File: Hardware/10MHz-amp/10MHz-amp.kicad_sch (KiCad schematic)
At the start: 65 parts, among them J1 Conn_Coaxial, J3 Conn_Coaxial, J4 Barrel_Jack_MountingPin, K1 TQ2-24V, K2 TQ2-24V, K3 TQ2-24V, K4 TQ2-24V, K5 TQ2-24V, Q1 PMOS, SW1 SW_SP5T_NR01105, SW2 SW_SPDT, U1 THS3491xDDA

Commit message: added power management circuit
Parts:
- added C11, C12: 10u, Capacitor_SMD:C_0603_1608Metric, symbol Device:C
- added C19, C20: 6.8u, Capacitor_SMD:C_0603_1608Metric, symbol Device:C
- added C21, C22, C23, C24, C25, C26: 100n, Capacitor_SMD:C_0603_1608Metric, symbol Device:C
- added C27: 1u, Capacitor_SMD:C_0603_1608Metric, symbol Device:C
- added C8, C9: 22u, Capacitor_SMD:C_0603_1608Metric, symbol Device:C
- added D1, D2: PTVS15VZ1USK, Diode_SMD:Nexperia_DSN1608-2_1.6x0.8mm, symbol Diode:PTVS15VZ1USK
- added D10, D21, D22, D7, D9: LED, Diode_SMD:D_0603_1608Metric, symbol Device:LED
- added D4, D5: D_Zener, Diode_SMD:D_0603_1608Metric, symbol Device:D_Zener
- added F1, F2: Fuse, symbol Device:Fuse
- added J2, J3: BANANA_JACK, symbol Connector:Conn_01x01_Socket
- added J6: Conn_01x07_Pin, Connector_PinHeader_2.54mm:PinHeader_1x07_P2.54mm_Horizontal, symbol Connector:Conn_01x07_Pin
- added J7: Conn_01x07_Socket, Connector_PinSocket_2.54mm:PinSocket_1x07_P2.54mm_Vertical, symbol Connector:Conn_01x07_Socket
- added J9: Conn_01x01_Socket, symbol Connector:Conn_01x01_Socket
- added JP2: Jumper_2_Bridged, symbol Jumper:Jumper_2_Bridged
- added Q1: PMOS, symbol Simulation_SPICE:PMOS
- added Q2: NMOS, symbol Simulation_SPICE:NMOS
- added Q4, Q5: AO4803A, SO8SOP-8L_AOS, symbol 2025-08-14_00-39-45:AO4803A
- added R10, R15, R16, R35, R36, R37, R7, R8: 10k, Capacitor_SMD:C_0603_1608Metric, symbol Device:R
- added R27, R28, R29, R30, R31, R32, R33, R34: 1M, Capacitor_SMD:C_0603_1608Metric, symbol Device:R
- added R38, R39: 0, symbol Device:R
- added SW3: SW_SPDT, symbol Switch:SW_SPDT
- added U2: LTC4417HGN, Package_SO:SSOP-24_3.9x8.7mm_P0.635mm, symbol Power_Management:LTC4417HGN
- C1: renamed from C3; footprint (none) -> Capacitor_SMD:C_0603_1608Metric
- C10: renamed from C5; footprint (none) -> Capacitor_SMD:C_0603_1608Metric
- C13: renamed from C6; footprint (none) -> Capacitor_SMD:C_0603_1608Metric
- C14: renamed from C7; footprint (none) -> Capacitor_SMD:C_0603_1608Metric
- C15: renamed from C8; footprint (none) -> Capacitor_SMD:C_0603_1608Metric
- C16: renamed from C9; footprint (none) -> Capacitor_SMD:C_0603_1608Metric
- C17: renamed from C10; footprint (none) -> Capacitor_SMD:C_0603_1608Metric
- C18: renamed from C11; footprint (none) -> Capacitor_SMD:C_0603_1608Metric
- C2, R11, R4, R5, R6, R9: footprint (none) -> Capacitor_SMD:C_0603_1608Metric
- C3: renamed from C1; footprint (none) -> Capacitor_SMD:C_0603_1608Metric
- C4: renamed from C12; footprint (none) -> Capacitor_SMD:C_0603_1608Metric
- C5: renamed from C13; footprint (none) -> Capacitor_SMD:C_0603_1608Metric
- C6: renamed from C14; footprint (none) -> Capacitor_SMD:C_0603_1608Metric
- C7: renamed from C4; footprint (none) -> Capacitor_SMD:C_0603_1608Metric
- D11: renamed from D7; footprint (none) -> Diode_SMD:D_0603_1608Metric
- D12: renamed from D6; footprint (none) -> Diode_SMD:D_0603_1608Metric
- D13: renamed from D5; footprint (none) -> Diode_SMD:D_0603_1608Metric
- D14: renamed from D4; footprint (none) -> Diode_SMD:D_0603_1608Metric
- D15: renamed from D3; footprint (none) -> Diode_SMD:D_0603_1608Metric
- D16: renamed from D9; footprint (none) -> Diode_SMD:D_0603_1608Metric; Notes (none) -> ADJ GAIN
- D17: renamed from D10; footprint (none) -> Diode_SMD:D_0603_1608Metric; Notes (none) -> 2x
- D18: renamed from D11; footprint (none) -> Diode_SMD:D_0603_1608Metric; Notes (none) -> 10x
- D19: renamed from D12; footprint (none) -> Diode_SMD:D_0603_1608Metric; Notes (none) -> 50x
- D20: renamed from D13; footprint (none) -> Diode_SMD:D_0603_1608Metric; Notes (none) -> 100x
- D6: renamed from D1; footprint (none) -> Diode_SMD:D_0603_1608Metric
- D8: footprint (none) -> Diode_SMD:D_0603_1608Metric; Notes (none) -> POWER
- JP1: value star_point -> Jumper_2_Bridged
- N1: value Housing_Pad -> Housing
- R1: renamed from R8; footprint (none) -> Capacitor_SMD:C_0603_1608Metric; Notes (none) -> LOAD RESISTOR 18w
- R12: renamed from R7; footprint (none) -> Capacitor_SMD:C_0603_1608Metric
- R13: renamed from R10; footprint (none) -> Capacitor_SMD:C_0603_1608Metric
- R14: renamed from R16; footprint (none) -> Capacitor_SMD:C_0603_1608Metric
- R17: renamed from R1; footprint (none) -> Capacitor_SMD:C_0603_1608Metric
- R18: renamed from R12; footprint (none) -> Capacitor_SMD:C_0603_1608Metric
- R19: renamed from R13; footprint (none) -> Capacitor_SMD:C_0603_1608Metric
- R2: renamed from R3; footprint (none) -> Potentiometer_THT:Potentiometer_Alps_RK09Y11_Single_Horizontal
- R20: renamed from R14; footprint (none) -> Capacitor_SMD:C_0603_1608Metric
- R21: renamed from R15; footprint (none) -> Capacitor_SMD:C_0603_1608Metric
- R22: renamed from R17; footprint (none) -> Capacitor_SMD:C_0603_1608Metric
- R23: renamed from R18; footprint (none) -> Capacitor_SMD:C_0603_1608Metric
- R24: renamed from R19; footprint (none) -> Capacitor_SMD:C_0603_1608Metric
- R25: renamed from R20; footprint (none) -> Capacitor_SMD:C_0603_1608Metric
- R26: renamed from R21; footprint (none) -> Capacitor_SMD:C_0603_1608Metric
- R3: renamed from R2; footprint (none) -> Capacitor_SMD:C_0603_1608Metric
- renumbered D2 to D3, F1 to F3, J3 to J5, JP2 to JP3, Q1 to Q3, SW2 to SW1, SW1 to SW2
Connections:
- net +24V: now also C23.1, C26.1, J7.1 (Pin_1), Q5.7, Q5.8, R29.2, U2.23 (V2); no longer C1.1, C18.1, C2.1, C3.1, R12.2, SW2.C (Common), U1.7 (V+)
- net -VDC: now also C12.2, C9.2, D10.1 (K), JP2.2 (B); no longer C1.2, C10.2, C13.2, C14.2, C15.2, C16.2, C17.2, C18.2, C2.2, C3.2, C4.1, C4.2, C5.1, C5.2, C6.1, C6.2, C7.2, D3.3 (A), J1.2 (Ext), J4.2, J5.2 (Ext), JP1.1 (A), R1.2, R14.1, R17.1, R18.1, R19.1, R2.2, R20.1, R21.1, R22.1, R23.1, R24.1, R25.1, R26.1, R3.2, R4.2, R5.2, R6.2, R9.1, SW1.3 (C), U1.1 (REF), U1.4 (V-), U1.9 (EP)
- net GNDS: now also R38.1
- net at C17.1, D15.1 (K), D20.2 (A)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: now also J7.6 (Pin_6); no longer SW2.5
- net at C16.1, D14.1 (K), D19.2 (A)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: now also J7.5 (Pin_5); no longer SW2.4
- net at R1.1, U1.3 (+): now also C27.2; no longer J1.1 (In)
- net at C13.1, D11.1 (K), D16.2 (A)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: now also J7.2 (Pin_2); no longer SW2.1
- net at SW1.2 (B), U1.8 (~{PD}): now also D7.2 (A)
- net at C14.1, D12.1 (K), D17.2 (A)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: now also J7.3 (Pin_3); no longer SW2.2
- net at C15.1, D13.1 (K), D18.2 (A)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: now also J7.4 (Pin_4); no longer SW2.3
- net at SW2.MP: now also J6.7 (Pin_7); no longer JP1.2 (B)
- new net: Q4.1, Q4.3, U2.21 (VS1)
- new net: C21.1, Q4.2, Q4.4, U2.20 (G1)
- new net: D9.1 (K), R15.2
- new net: D4.1 (K), JP1.1 (A), Q1.3 (S)
- new net: J6.2 (Pin_2), SW2.1
- new net: J6.3 (Pin_3), SW2.2
- new net: J6.4 (Pin_4), SW2.3
- new net: J6.5 (Pin_5), SW2.4
- new net: J6.6 (Pin_6), SW2.5
- new net: C18.1, J6.1 (Pin_1), SW2.C (Common)
- new net: C22.1, Q5.2, Q5.4, U2.18 (G2)
- new net: SW3.2 (B), U2.2 (~{SHDN})
- new net: R37.2, SW3.3 (C)
- new net: D10.2 (A), R16.1
- new net: D21.2 (A), R35.1
- new net: R28.1, R35.2, U2.11 (~{VALID2})
- new net: C24.2, R32.1, R34.2, U2.5 (OV1)
- new net: F2.2, Q2.1 (D)
- new net: D5.1 (K), Q2.2 (G), R8.1
- new net: D5.2 (A), JP2.1 (A), Q2.3 (S)
- new net: J9.1 (Pin_1), R39.2
- new net: D7.1 (K), R10.2
- new net: D2.1 (K), F2.1, J3.1 (Pin_1)
- new net: R27.1, R36.2, U2.10 (~{VALID1})
- new net: Q5.1, Q5.3, U2.19 (VS2)
- new net: R31.1, R32.2, U2.4 (UV1)
- new net: R29.1, R30.2, U2.6 (UV2)
- new net: C23.2, R30.1, R33.2, U2.7 (OV2)
- new net: D22.2 (A), R36.1
- new net: D1.2 (A), F1.1, J2.1 (Pin_1)
- new net: F1.2, Q1.1 (D)
- new net: D4.2 (A), Q1.2 (G), R7.2
- new net: C27.1, J1.1 (In)
- new net +VDC: C11.1, C24.1, C25.1, C8.1, D9.2 (A), JP1.2 (B), Q4.7, Q4.8, R31.2, U2.24 (V1)
- new net GND: C1.2, C10.2, C11.2, C12.1, C13.2, C14.2, C15.2, C16.2, C17.2, C18.2, C19.2, C2.2, C20.2, C21.2, C22.2, C25.2, C26.2, C3.2, C4.2, C5.2, C6.2, C7.2, C8.2, C9.1, D1.1 (K), D2.2 (A), D21.1 (K), D22.1 (K), D3.3 (A), J1.2 (Ext), J4.2, J5.2 (Ext), J7.7 (Pin_7), R1.2, R10.1, R14.1, R15.1, R16.2, R17.1, R18.1, R19.1, R2.2, R20.1, R21.1, R22.1, R23.1, R24.1, R25.1, R26.1, R3.2, R33.1, R34.1, R37.1, R38.2, R39.1, R4.2, R5.2, R6.2, R7.1, R8.2, R9.1, SW1.3 (C), U1.1 (REF), U1.9 (EP), U2.13 (GND), U2.16 (G3), U2.17 (VS3), U2.22 (V3), U2.3 (HYS), U2.8 (UV3), U2.9 (OV3)
- new net VCC: C1.1, C19.1, C2.1, C20.1, C3.1, Q4.5, Q4.6, Q5.5, Q5.6, R12.2, R27.2, R28.2, U1.7 (V+), U2.15 (VOUT)
- new net VS: C4.1, C5.1, C6.1, U1.4 (V-)
- no-connect marks 21 -> 23
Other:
- note added: "24v @ 2A INPUT"
- note added: "DUAL RAIL +-15VMAX @ 500mA INPUT"
- note added: "POWER AMP 100MHz 30V pk-pk 500mA 50OHM LOAD"
- note added: "POWER SELECTOR"
- note added: "STAR GROUND POINT"
- moved on the sheet: C1, C10, C13, C14, C15, C16, C17, C18, C2, C3, C4, C5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

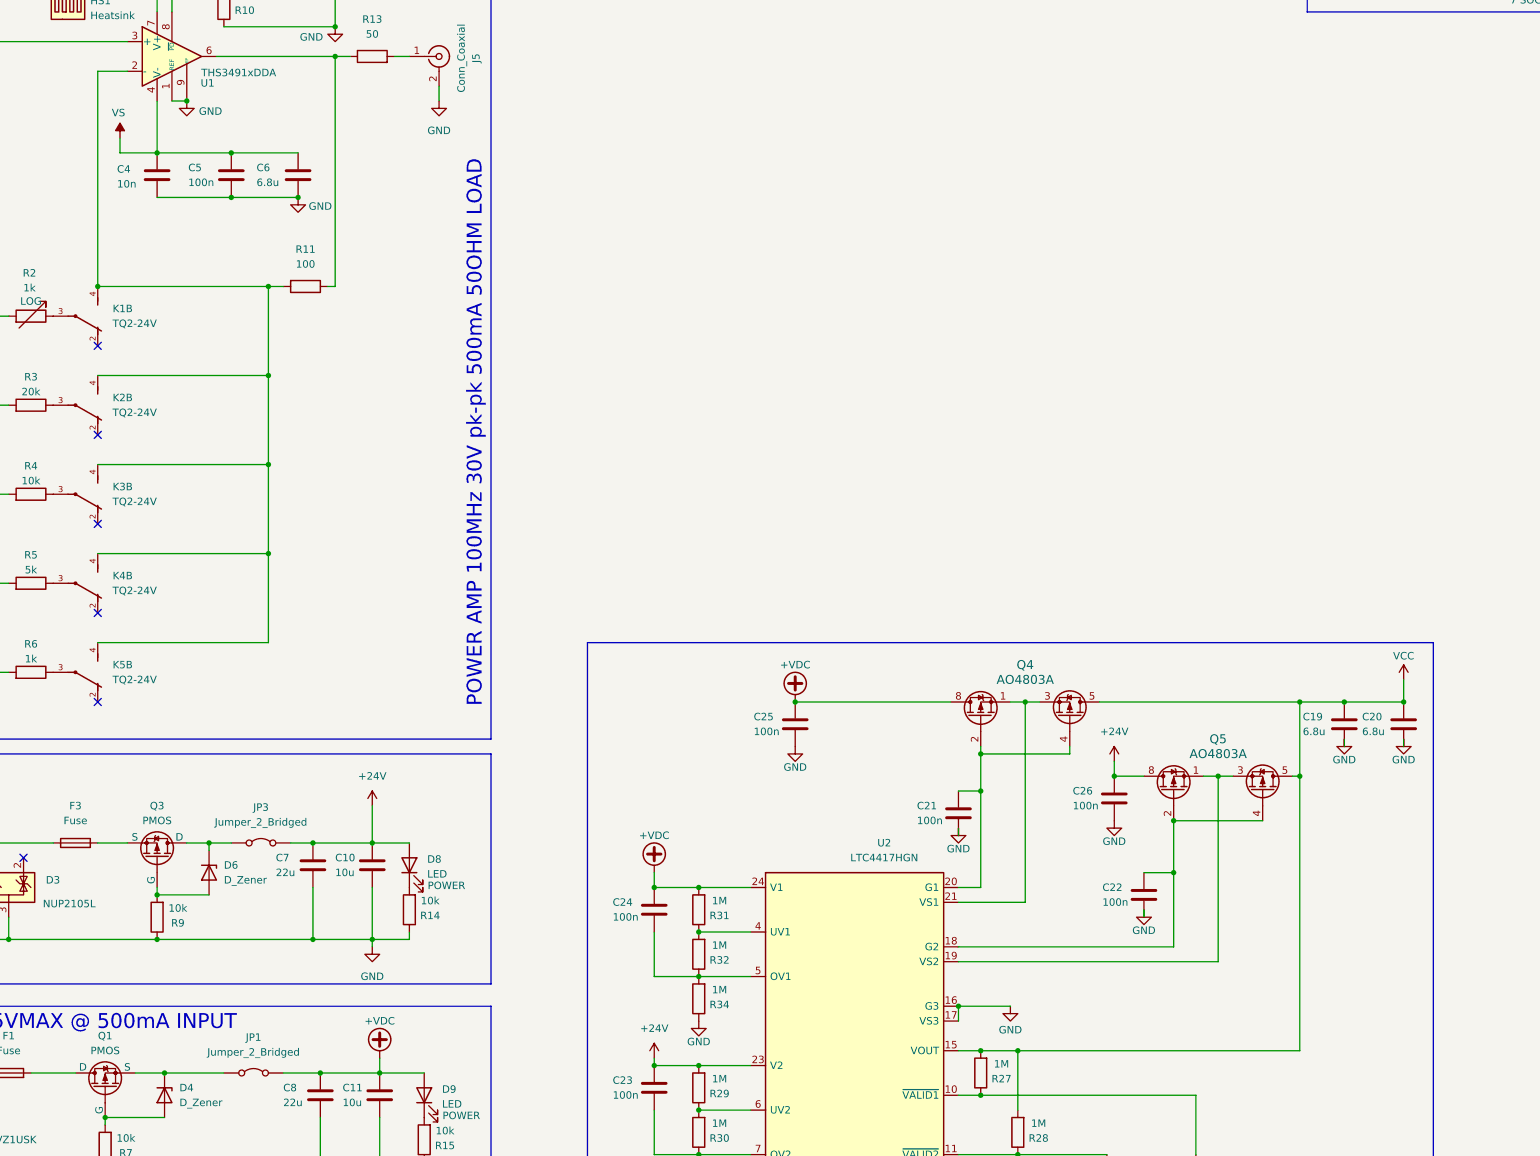
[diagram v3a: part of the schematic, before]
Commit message: added VS switcher circuit, so when +VDC is present then VS == -VDC if +VDC is not present then VS == GND
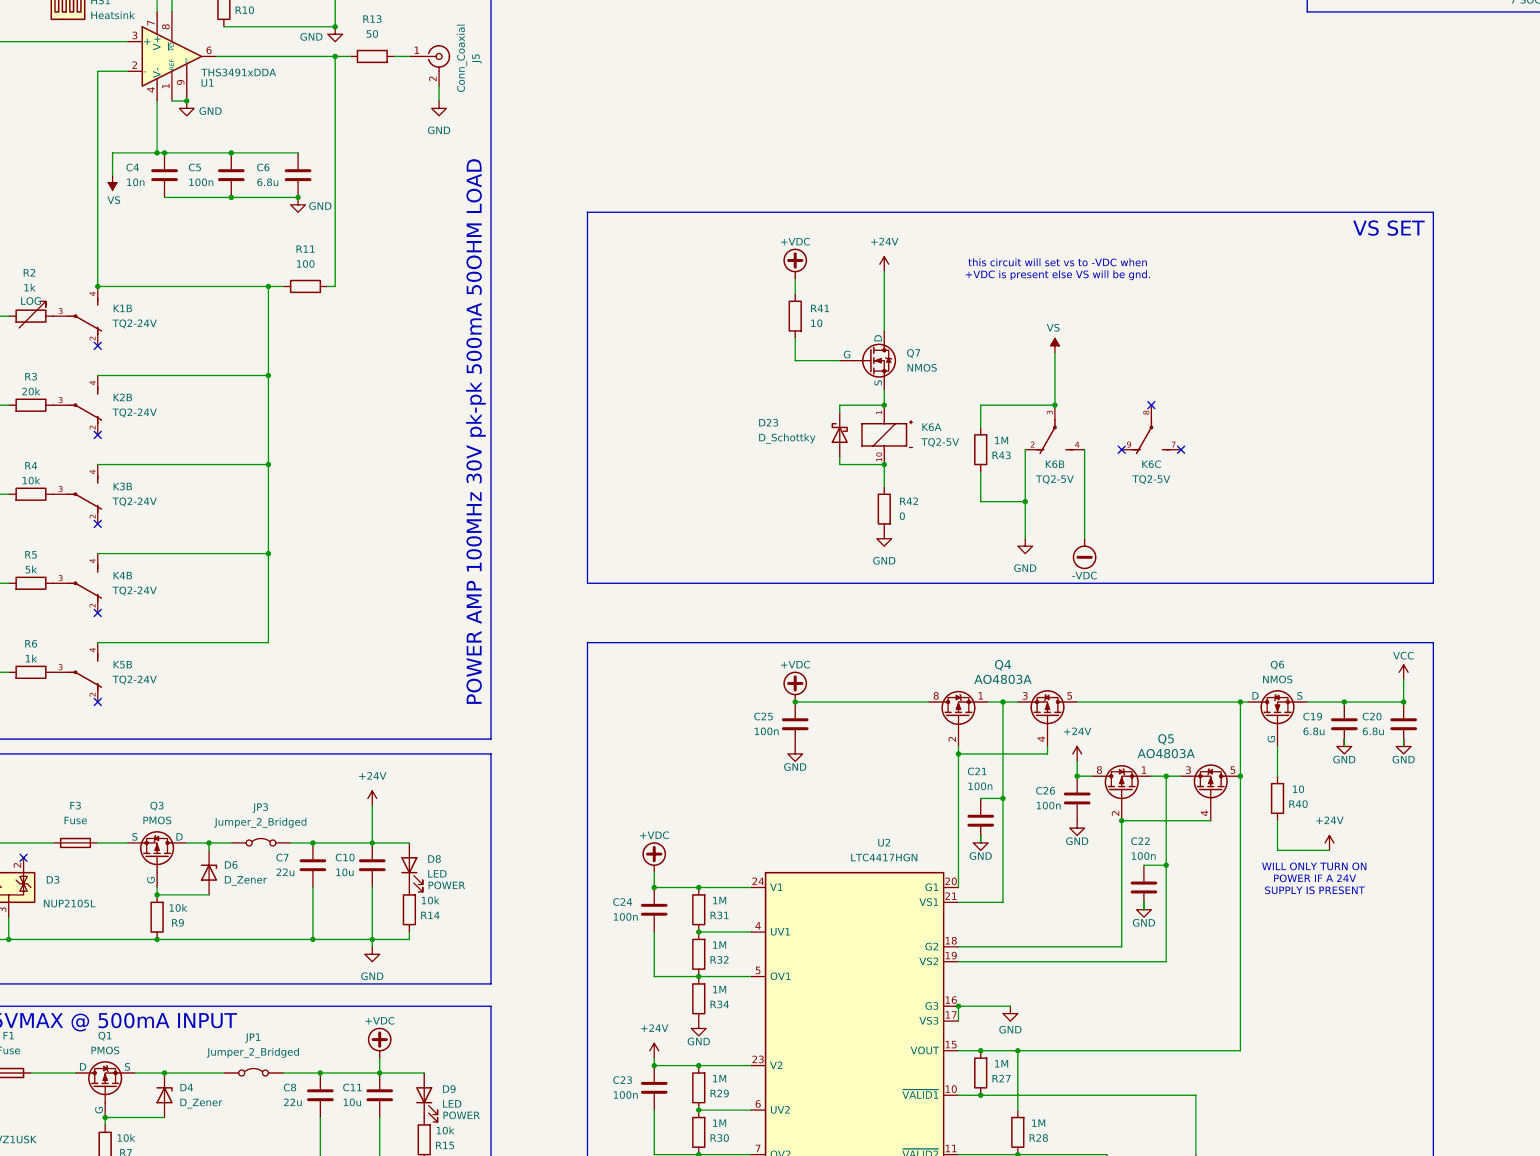
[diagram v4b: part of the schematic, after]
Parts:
- added D23: D_Schottky, Diode_SMD:D_0603_1608Metric, symbol Device:D_Schottky
- added K6: TQ2-5V, TQ2-5V:TQ2, symbol TQ2-5V:TQ2-5V
- added Q6, Q7: NMOS, symbol Simulation_SPICE:NMOS
- added R40, R41: 10, Capacitor_SMD:C_0603_1608Metric, symbol Device:R
- added R42: 0, Capacitor_SMD:C_0603_1608Metric, symbol Device:R
- added R43: 1M, Capacitor_SMD:C_0603_1608Metric, symbol Device:R
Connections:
- net +24V: now also Q7.1 (D), R40.1
- net +VDC: now also R41.1
- net -VDC: now also K6.4
- net GND: now also K6.2, R42.2, R43.1
- net VCC: now also Q6.3 (S); no longer Q4.5, Q4.6, Q5.5, Q5.6, R27.2, R28.2, U2.15 (VOUT)
- net VS: now also K6.3, R43.2
- net at Q4.1, Q4.3, U2.21 (VS1): now also C21.1
- net at Q4.2, Q4.4, U2.20 (G1): no longer C21.1
- net at Q5.2, Q5.4, U2.18 (G2): no longer C22.1
- net at Q5.1, Q5.3, U2.19 (VS2): now also C22.1
- new net: D23.1 (K), K6.1, Q7.3 (S)
- new net: D23.2 (A), K6.10, R42.1
- new net: Q4.5, Q4.6, Q5.5, Q5.6, Q6.1 (D), R27.2, R28.2, U2.15 (VOUT)
- new net: Q6.2 (G), R40.2
- new net: Q7.2 (G), R41.2
- no-connect marks 23 -> 26
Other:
- note added: "VS SET"
- note added: "WILL ONLY TURN ON POWER IF A 24V SUPPLY IS PRESENT"
- note added: "this circuit will set vs to -VDC when +VDC is present else VS will be gnd."
- moved on the sheet: C21, C22, C26, C4, Q4, Q5

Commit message: removed power swapping circuit and replaced with switch and relay because it was going to be too much to a pain to make work
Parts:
- removed C19, C20: 6.8u, Capacitor_SMD:C_0603_1608Metric, symbol Device:C
- removed C21, C22, C24, C25, C26: 100n, Capacitor_SMD:C_0603_1608Metric, symbol Device:C
- removed C27: 1u, Capacitor_SMD:C_0603_1608Metric, symbol Device:C
- removed C8: 22u, Capacitor_SMD:C_0603_1608Metric, symbol Device:C
- removed D1, D2: PTVS15VZ1USK, Diode_SMD:Nexperia_DSN1608-2_1.6x0.8mm, symbol Diode:PTVS15VZ1USK
- removed D21, D22: LED, Diode_SMD:D_0603_1608Metric, symbol Device:LED
- removed D3: NUP2105L, Package_TO_SOT_SMD:SOT-23, symbol Power_Protection:NUP2105L
- removed J9: Conn_01x01_Socket, symbol Connector:Conn_01x01_Socket
- removed Q4, Q5: AO4803A, SO8SOP-8L_AOS, symbol 2025-08-14_00-39-45:AO4803A
- removed Q6, Q7: NMOS, symbol Simulation_SPICE:NMOS
- removed R27, R28, R29, R30, R33, R34, R43: 1M, Capacitor_SMD:C_0603_1608Metric, symbol Device:R
- removed R35, R36, R37: 10k, Capacitor_SMD:C_0603_1608Metric, symbol Device:R
- removed R40, R41: 10, Capacitor_SMD:C_0603_1608Metric, symbol Device:R
- removed SW3: SW_SPDT, symbol Switch:SW_SPDT
- removed U2: LTC4417HGN, Package_SO:SSOP-24_3.9x8.7mm_P0.635mm, symbol Power_Management:LTC4417HGN
- added C10: 10u, Capacitor_SMD:C_0603_1608Metric, symbol Device:C
- added C13, C17: 100n, Capacitor_SMD:C_0603_1608Metric, symbol Device:C
- added C14, C16: 6.8u, Capacitor_SMD:C_0603_1608Metric, symbol Device:C
- added D1, D11, D12, D2: SM15T39A, Diode_SMD:ST_D_SMC, symbol Diode:SM15T36A
- added D26: LED, Diode_SMD:D_0603_1608Metric, symbol Device:LED
- added D3, D4: PTVS18VZ1USK, Diode_SMD:Nexperia_DSN1608-2_1.6x0.8mm, symbol Diode:PTVS18VZ1USK
- added D5: PTVS15VZ1USK, Diode_SMD:Nexperia_DSN1608-2_1.6x0.8mm, symbol Diode:PTVS15VZ1USK
- added J4: BANANA_JACK, symbol Connector:Conn_01x01_Socket
- added R23: 0, symbol Device:R
- added SW2: SW_SPST, symbol Switch:SW_SPST
- added TP1, TP2: grounding_strip, symbol Connector:TestPoint
- C1, C12, C2, C3, C4, C5, C6, C7, C9: Notes (none) -> 35v
- C11: value 10u -> 22u; Notes (none) -> 35v
- C8: renamed from C10; Notes (none) -> 35v
- R31: value 1M -> 0; footprint Capacitor_SMD:C_0603_1608Metric -> (none)
- R32: value 1M -> 10k
- renumbered C18 to C15, C13 to C18, C14 to C19, C15 to C20, C16 to C21, C17 to C22, D8 to D10, D9 to D13, D10 to D14, D23 to D15, D11 to D21, D12 to D22, D13 to D23, D14 to D24, D15 to D25, D4 to D8, D5 to D9, F3 to F1, F1 to F2, F2 to F3, J4 to J2, J2 to J3, J3 to J5, J5 to J6, J6 to J7, J7 to J8, JP3 to JP1, JP1 to JP2, JP2 to JP3, Q3 to Q1, Q1 to Q2, Q2 to Q3, R8 to R10, R42 to R17, R22 to R18, R23 to R19, R24 to R20, R25 to R21, R26 to R22, R17 to R24, R18 to R25, R19 to R26, R20 to R27, R21 to R28, R39 to R29, R38 to R30, R9 to R7, R10 to R8, R7 to R9, SW2 to SW3
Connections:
- net +24V: now also K6.9, D26.2 (A), SW2.1 (A); no longer C23.1
- net +VDC: now also C9.1, K6.7, C10.1; no longer C11.1, R31.2
- net -VDC: now also C11.2; no longer C9.2
- net GND: now also C11.1, C23.2, C9.2, R30.1, R32.1, C10.2, C13.2, C14.2, C16.2, C17.2, D3.2 (A), D4.1 (K), D5.2 (A); no longer C11.2, C9.1, J2.2, R29.1, R30.2
- net GNDS: now also R23.1; no longer R30.1
- net VCC: now also K6.8, C16.1, C17.1, D1.1 (A1), D11.1 (A1)
- net VS: now also C13.1, C14.1, D12.2 (A2), D2.2 (A2)
- net at C22.1, D25.1 (K), J8.6 (Pin_6)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: no longer D20.2 (A)
- net at C21.1, D24.1 (K), J8.5 (Pin_5)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: no longer D19.2 (A)
- net at D15.1 (K), K6.1: now also C23.1, SW2.2 (B)
- net at R1.1, U1.3 (+): now also J1.1 (In), D1.2 (A2), D2.1 (A1)
- net at C18.1, D21.1 (K), J8.2 (Pin_2)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: no longer D16.2 (A)
- net at F1.2, Q1.3 (S): now also D5.1 (K)
- net at J7.2 (Pin_2), SW3.1: now also D16.2 (A)
- net at J7.3 (Pin_3), SW3.2: now also D17.2 (A)
- net at J7.4 (Pin_4), SW3.3: now also D18.2 (A)
- net at J7.5 (Pin_5), SW3.4: now also D19.2 (A)
- net at J7.7 (Pin_7), SW3.MP: now also D20.2 (A)
- net at J6.1 (In), R13.2: now also D11.2 (A2), D12.1 (A1)
- net at C20.1, D23.1 (K), J8.4 (Pin_4)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: no longer D18.2 (A)
- net at C19.1, D22.1 (K), J8.3 (Pin_3)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: no longer D17.2 (A)
- net at F3.2, Q3.1 (D): now also D4.2 (A)
- net GND1: now reaches R29.2
- net GND1: now also J4.1 (Pin_1)
- net at R32.2: now also D26.1 (K); no longer R31.1
- net at F2.2, Q2.1 (D): now also D3.1 (K)
- new net: R23.2, R29.1, R30.2, R31.2
- new net GND2: J2.2, R31.1
- no-connect marks 26 -> 21
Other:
- note added: "POWER SWAP"
- note removed: "POWER SELECTOR"
- note removed: "VS SET"
- note removed: "WILL ONLY TURN ON POWER IF A 24V SUPPLY IS PRESENT"
- note removed: "this circuit will set vs to -VDC when +VDC is present else VS will be gnd."
- moved on the sheet: C1, C15, C18, C19, C2, C20, C21, C22, C3, D13, D14, D15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

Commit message: added more context to blocks
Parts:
- removed JP1, JP2, JP3: Jumper_2_Bridged, symbol Jumper:Jumper_2_Bridged
- added FB1, FB2, FB3: FerriteBead, symbol Device:FerriteBead
- added JP1: 24V, symbol Jumper:Jumper_2_Open
- added JP2: +VDC, symbol Jumper:Jumper_2_Open
- added JP3: -VDC, symbol Jumper:Jumper_2_Open
- added JP4, JP5, JP6: RVP BYPASS, symbol Jumper:Jumper_2_Open
- C13, C14, C16, C17, C18, C19, C20, C21, C22, C23: Notes (none) -> 35v
- D15, D21, D22, D23, D24, D25: Manufactor Part Number (none) -> NSR0340HT1G; Notes (none) -> 40 V 250mA; Supplier Part Number (none) -> NSR0340HT1GOSCT-ND; Supplier link (none) -> https://www.digikey.co.nz/en/products/detail/onsemi/NSR0340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
- D7: Notes (none) -> AMP EN
- K1, K2, K3, K4, K5: Notes 40ma -> 12.5 mA
- R1: Notes LOAD RESISTOR 18w -> 18w
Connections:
- net +24V: now also FB1.2
- net +VDC: now also FB2.2
- net -VDC: now also FB3.2
- net GND: now also K1.2, K1.3, K1.7, K1.8, K1.9, K2.2, K2.3, K2.7, K2.8, K2.9, K3.2, K3.3, K3.7, K3.8, K3.9, K4.2, K4.3, K4.7, K4.8, K4.9, K5.2, K5.3, K5.7, K5.8, K5.9; no longer R2.2, R3.2, R4.2, R5.2, R6.2
- net VCC: now also C23.1; no longer C17.1
- net VS: now also C17.1; no longer C13.1
- net at R5.1: now also R11.2, R2.1, R3.1, R4.1, R6.1, U1.2 (-); no longer K4.3
- net at D15.1 (K), K6.1, SW2.2 (B): now also C13.1; no longer C23.1
- net at D6.1 (K), Q1.1 (D): now also JP1.1 (A), JP4.2 (B)
- net at D5.1 (K), F1.2, Q1.3 (S): now also JP4.1 (A)
- net at D8.1 (K), Q2.3 (S): now also JP2.1 (A), JP5.2 (B)
- net at D4.2 (A), F3.2, Q3.1 (D): now also JP6.1 (A)
- net at D3.1 (K), F2.2, Q2.1 (D): now also JP5.1 (A)
- net at D9.2 (A), Q3.3 (S): now also JP3.1 (A), JP6.2 (B)
- new net: K4.4, R5.2
- new net: K5.4, R6.2
- new net: K2.4, R3.2
- new net: K1.4, R2.2
- new net: K3.4, R4.2
- new net: FB1.1, JP1.2 (B)
- new net: FB2.1, JP2.2 (B)
- new net: FB3.1, JP3.2 (B)
- no-connect marks 21 -> 2
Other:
- note added: "50 Ohm LOAD"
- note added: "50 Ohm termination"
- note added: "ESD PROTECTION"
- note added: "FUSE"
- note added: "GAIN SELECT SWTICH"
- note added: "GND --- HS SIG --- GND --- LS SIG / PWR"
- note added: "POWER STATUS"
- note added: "RVP"
- note added: "TVS"
- note added: "VCC LOAD SIDE"
- note added: "VS LOAD SIDE"
- note added: "decoupling"
- note added: "power"
- note added: "stack up"
- note added: "switch"
- note added: "test point"
- moved on the sheet: C10, C11, C12, C15, C18, C7, C8, C9, D10, D13, D14, D15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
